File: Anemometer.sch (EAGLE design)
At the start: 1 part, among them IC1 TINY2313-*S*

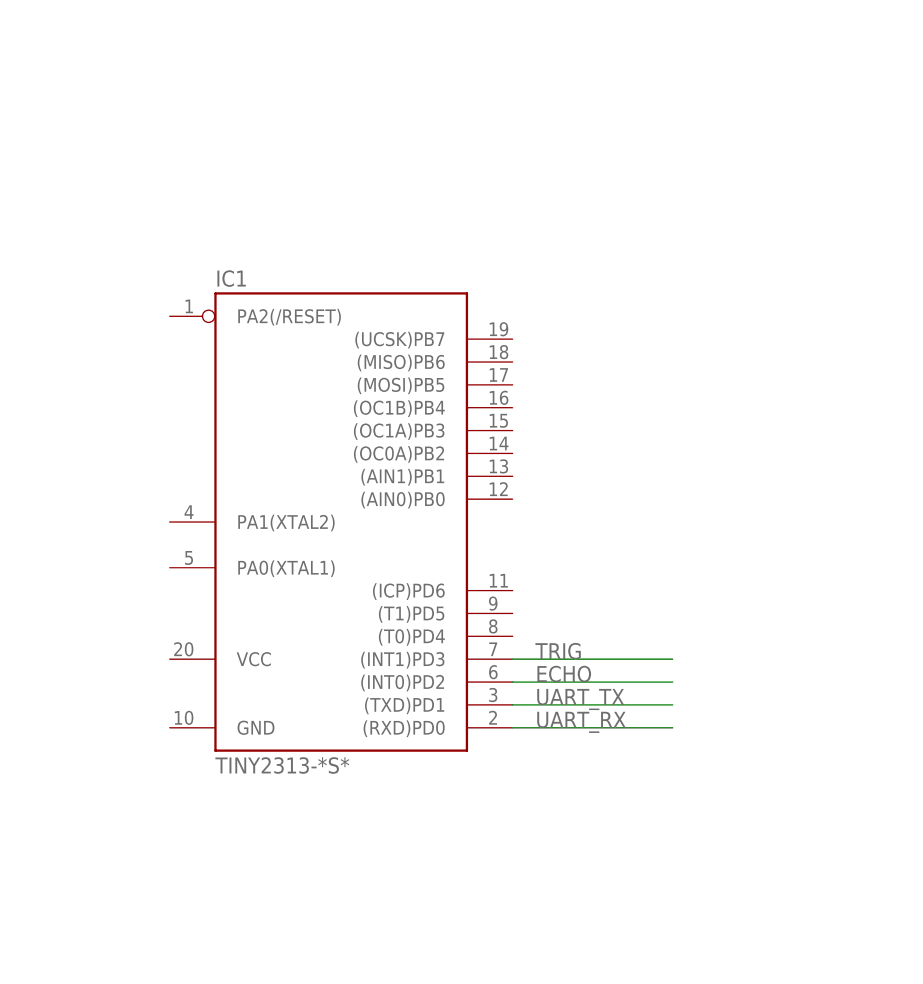
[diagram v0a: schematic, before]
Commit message: added Houskeeping to Schematic
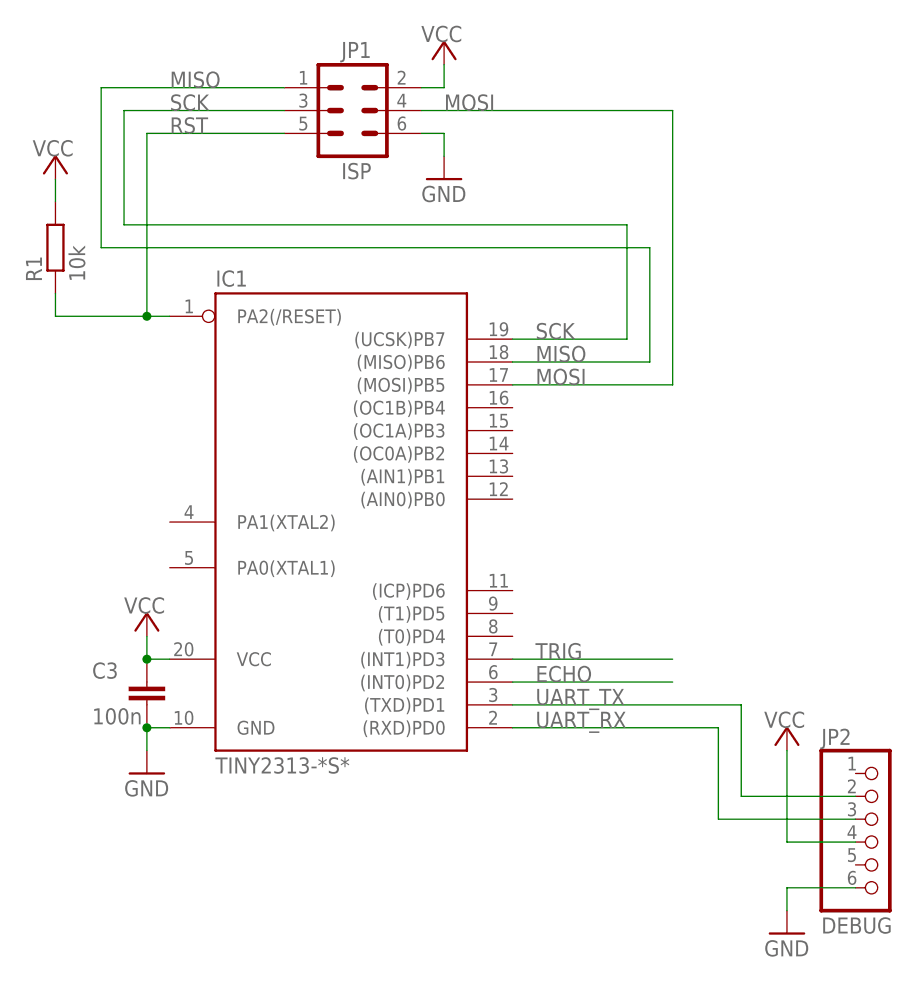
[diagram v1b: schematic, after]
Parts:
- added C3: 100n, rcl:C-EU050-024X044
- added JP1: ISP, con-harting-ml:ML6
- added JP2: DEBUG, pinhead:PINHD-1X6
- added R1: 10k, rcl:R-EU_0207/10
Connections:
- new net GND: C3.2, IC1.GND, JP1.6, JP2.6
- new net MISO: IC1.(MISO)PB6, JP1.1
- new net MOSI: IC1.(MOSI)PB5, JP1.4
- new net RST: IC1.PA2(/RESET), JP1.5, R1.1
- new net SCK: IC1.(UCSK)PB7, JP1.3
- new net VCC: C3.1, IC1.VCC, JP1.2, JP2.4, R1.2
- net UART_RX: now also JP2.3
- net UART_TX: now also JP2.2
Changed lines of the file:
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@@
 <parts>
 <part name="IC1" library="avr-7" deviceset="TINY2313*" device="-*S*"/>
+<part name="JP1" library="con-harting-ml" library_urn="urn:adsk.eagle:library:149" deviceset="ML6" device="" package3d_urn="urn:adsk.eagle:package:6988/1" value="ISP"/>
+<part name="R1" library="rcl" library_urn="urn:adsk.eagle:library:334" deviceset="R-EU_" device="0207/10" package3d_urn="urn:adsk.eagle:package:23491/2" value="10k"/>
+<part name="GND1" library="supply1" library_urn="urn:adsk.eagle:library:371" deviceset="GND" device=""/>
+<part name="GND2" library="supply1" library_urn="urn:adsk.eagle:library:371" deviceset="GND" device=""/>
+<part name="P+1" library="supply1" library_urn="urn:adsk.eagle:library:371" deviceset="VCC" device=""/>
+<part name="P+2" library="supply1" library_urn="urn:adsk.eagle:library:371" deviceset="VCC" device=""/>
+<part name="P+3" library="supply1" library_urn="urn:adsk.eagle:library:371" deviceset="VCC" device=""/>
+<part name="JP2" library="pinhead" library_urn="urn:adsk.eagle:library:325" deviceset="PINHD-1X6" device="" package3d_urn="urn:adsk.eagle:package:22472/2" value="DEBUG"/>
+<part name="GND3" library="supply1" library_urn="urn:adsk.eagle:library:371" deviceset="GND" device=""/>
+<part name="P+4" library="supply1" library_urn="urn:adsk.eagle:library:371" deviceset="VCC" device=""/>
+<part name="C3" library="rcl" library_urn="urn:adsk.eagle:library:334" deviceset="C-EU" device="050-024X044" package3d_urn="urn:adsk.eagle:package:23643/1" value="100n"/>
 </parts>
 <sheets>
@@
 <attribute name="NAME" x="-15.24" y="23.622" size="1.778" layer="95"/>
 </instance>
+<instance part="JP1" gate="1" x="0" y="43.18" smashed="yes" rot="R180">
+<attribute name="VALUE" x="-1.27" y="35.56" size="1.778" layer="96"/>
+<attribute name="NAME" x="-1.27" y="49.022" size="1.778" layer="95"/>
+</instance>
+<instance part="R1" gate="G$1" x="-33.02" y="27.94" smashed="yes" rot="R90">
+<attribute name="NAME" x="-34.5186" y="24.13" size="1.778" layer="95" rot="R90"/>
+<attribute name="VALUE" x="-29.718" y="24.13" size="1.778" layer="96" rot="R90"/>
+</instance>
+<instance part="GND1" gate="1" x="-22.86" y="-30.48" smashed="yes">
+<attribute name="VALUE" x="-25.4" y="-33.02" size="1.778" layer="96"/>
+</instance>
+<instance part="GND2" gate="1" x="10.16" y="35.56" smashed="yes">
+<attribute name="VALUE" x="7.62" y="33.02" size="1.778" layer="96"/>
+</instance>
+<instance part="P+1" gate="VCC" x="-33.02" y="38.1" smashed="yes">
+<attribute name="VALUE" x="-35.56" y="38.1" size="1.778" layer="96"/>
+</instance>
+<instance part="P+2" gate="VCC" x="10.16" y="50.8" smashed="yes">
+<attribute name="VALUE" x="7.62" y="50.8" size="1.778" layer="96"/>
+</instance>
+<instance part="P+3" gate="VCC" x="-22.86" y="-12.7" smashed="yes">
+<attribute name="VALUE" x="-25.4" y="-12.7" size="1.778" layer="96"/>
+</instance>
+<instance part="JP2" gate="A" x="58.42" y="-38.1" smashed="yes">
+<attribute name="NAME" x="52.07" y="-27.305" size="1.778" layer="95"/>
+<attribute name="VALUE" x="52.07" y="-48.26" size="1.778" layer="96"/>
+</instance>
+<instance part="GND3" gate="1" x="48.26" y="-48.26" smashed="yes">
+<attribute name="VALUE" x="45.72" y="-50.8" size="1.778" layer="96"/>
+</instance>
+<instance part="P+4" gate="VCC" x="48.26" y="-25.4" smashed="yes">
+<attribute name="VALUE" x="45.72" y="-25.4" size="1.778" layer="96"/>
+</instance>
+<instance part="C3" gate="G$1" x="-22.86" y="-20.32" smashed="yes">
+<attribute name="NAME" x="-28.956" y="-19.939" size="1.778" layer="95"/>
+<attribute name="VALUE" x="-28.956" y="-25.019" size="1.778" layer="96"/>
+</instance>
 </instances>
 <busses>
@@
 <segment>
 <pinref part="IC1" gate="G$1" pin="(TXD)PD1"/>
-<wire x1="17.78" y1="-22.86" x2="35.56" y2="-22.86" width="0.1524" layer="91"/>
+<wire x1="17.78" y1="-22.86" x2="43.18" y2="-22.86" width="0.1524" layer="91"/>
 <label x="20.32" y="-22.86" size="1.778" layer="95"/>
+<pinref part="JP2" gate="A" pin="2"/>
+<wire x1="55.88" y1="-33.02" x2="43.18" y2="-33.02" width="0.1524" layer="91"/>
+<wire x1="43.18" y1="-33.02" x2="43.18" y2="-22.86" width="0.1524" layer="91"/>
 </segment>
 </net>
@@
 <segment>
 <pinref part="IC1" gate="G$1" pin="(RXD)PD0"/>
-<wire x1="17.78" y1="-25.4" x2="35.56" y2="-25.4" width="0.1524" layer="91"/>
+<wire x1="17.78" y1="-25.4" x2="40.64" y2="-25.4" width="0.1524" layer="91"/>
 <label x="20.32" y="-25.4" size="1.778" layer="95"/>
+<pinref part="JP2" gate="A" pin="3"/>
+<wire x1="55.88" y1="-35.56" x2="40.64" y2="-35.56" width="0.1524" layer="91"/>
+<wire x1="40.64" y1="-35.56" x2="40.64" y2="-25.4" width="0.1524" layer="91"/>
+</segment>
+</net>
+<net name="MISO" class="0">
+<segment>
+<pinref part="JP1" gate="1" pin="1"/>
+<wire x1="-7.62" y1="45.72" x2="-27.94" y2="45.72" width="0.1524" layer="91"/>
+<label x="-20.32" y="45.72" size="1.778" layer="95"/>
+<wire x1="17.78" y1="15.24" x2="33.02" y2="15.24" width="0.1524" layer="91"/>
+<wire x1="33.02" y1="15.24" x2="33.02" y2="27.94" width="0.1524" layer="91"/>
+<wire x1="33.02" y1="27.94" x2="-27.94" y2="27.94" width="0.1524" layer="91"/>
+<wire x1="-27.94" y1="27.94" x2="-27.94" y2="45.72" width="0.1524" layer="91"/>
+<label x="20.32" y="15.24" size="1.778" layer="95"/>
+<pinref part="IC1" gate="G$1" pin="(MISO)PB6"/>
+</segment>
+</net>
+<net name="SCK" class="0">
+<segment>
+<pinref part="JP1" gate="1" pin="3"/>
+<wire x1="-7.62" y1="43.18" x2="-25.4" y2="43.18" width="0.1524" layer="91"/>
+<label x="-20.32" y="43.18" size="1.778" layer="95"/>
+<wire x1="17.78" y1="17.78" x2="30.48" y2="17.78" width="0.1524" layer="91"/>
+<wire x1="30.48" y1="17.78" x2="30.48" y2="30.48" width="0.1524" layer="91"/>
+<wire x1="30.48" y1="30.48" x2="-25.4" y2="30.48" width="0.1524" layer="91"/>
+<wire x1="-25.4" y1="30.48" x2="-25.4" y2="43.18" width="0.1524" layer="91"/>
+<label x="20.32" y="17.78" size="1.778" layer="95"/>
+<pinref part="IC1" gate="G$1" pin="(UCSK)PB7"/>
+</segment>
+</net>
+<net name="RST" class="0">
+<segment>
+<pinref part="JP1" gate="1" pin="5"/>
+<wire x1="-7.62" y1="40.64" x2="-22.86" y2="40.64" width="0.1524" layer="91"/>
+<label x="-20.32" y="40.64" size="1.778" layer="95"/>
+<wire x1="-20.32" y1="20.32" x2="-22.86" y2="20.32" width="0.1524" layer="91"/>
+<wire x1="-22.86" y1="20.32" x2="-22.86" y2="40.64" width="0.1524" layer="91"/>
+<pinref part="R1" gate="G$1" pin="1"/>
+<wire x1="-33.02" y1="22.86" x2="-33.02" y2="20.32" width="0.1524" layer="91"/>
+<wire x1="-33.02" y1="20.32" x2="-22.86" y2="20.32" width="0.1524" layer="91"/>
+<junction x="-22.86" y="20.32"/>
+<pinref part="IC1" gate="G$1" pin="PA2(/RESET)"/>
+</segment>
+</net>
+<net name="MOSI" class="0">
+<segment>
+<pinref part="JP1" gate="1" pin="4"/>
+<wire x1="7.62" y1="43.18" x2="35.56" y2="43.18" width="0.1524" layer="91"/>
+<label x="10.16" y="43.18" size="1.778" layer="95"/>
+<wire x1="17.78" y1="12.7" x2="35.56" y2="12.7" width="0.1524" layer="91"/>
+<wire x1="35.56" y1="12.7" x2="35.56" y2="43.18" width="0.1524" layer="91"/>
+<label x="20.32" y="12.7" size="1.778" layer="95"/>
+<pinref part="IC1" gate="G$1" pin="(MOSI)PB5"/>
+</segment>
+</net>
+<net name="GND" class="0">
+<segment>
+<pinref part="GND1" gate="1" pin="GND"/>
+<wire x1="-22.86" y1="-27.94" x2="-22.86" y2="-25.4" width="0.1524" layer="91"/>
+<wire x1="-22.86" y1="-25.4" x2="-20.32" y2="-25.4" width="0.1524" layer="91"/>
+<pinref part="C3" gate="G$1" pin="2"/>
+<junction x="-22.86" y="-25.4"/>
+<pinref part="IC1" gate="G$1" pin="GND"/>
+</segment>
+<segment>
+<pinref part="JP1" gate="1" pin="6"/>
+<pinref part="GND2" gate="1" pin="GND"/>
+<wire x1="7.62" y1="40.64" x2="10.16" y2="40.64" width="0.1524" layer="91"/>
+<wire x1="10.16" y1="40.64" x2="10.16" y2="38.1" width="0.1524" layer="91"/>
+</segment>
+<segment>
+<pinref part="JP2" gate="A" pin="6"/>
+<pinref part="GND3" gate="1" pin="GND"/>
+<wire x1="55.88" y1="-43.18" x2="48.26" y2="-43.18" width="0.1524" layer="91"/>
+<wire x1="48.26" y1="-43.18" x2="48.26" y2="-45.72" width="0.1524" layer="91"/>
+</segment>
+</net>
+<net name="VCC" class="0">
+<segment>
+<pinref part="P+3" gate="VCC" pin="VCC"/>
+<wire x1="-20.32" y1="-17.78" x2="-22.86" y2="-17.78" width="0.1524" layer="91"/>
+<wire x1="-22.86" y1="-17.78" x2="-22.86" y2="-15.24" width="0.1524" layer="91"/>
+<pinref part="C3" gate="G$1" pin="1"/>
+<junction x="-22.86" y="-17.78"/>
+<pinref part="IC1" gate="G$1" pin="VCC"/>
+</segment>
+<segment>
+<pinref part="R1" gate="G$1" pin="2"/>
+<pinref part="P+1" gate="VCC" pin="VCC"/>
+<wire x1="-33.02" y1="33.02" x2="-33.02" y2="35.56" width="0.1524" layer="91"/>
+</segment>
+<segment>
+<pinref part="JP1" gate="1" pin="2"/>
+<pinref part="P+2" gate="VCC" pin="VCC"/>
+<wire x1="7.62" y1="45.72" x2="10.16" y2="45.72" width="0.1524" layer="91"/>
+<wire x1="10.16" y1="45.72" x2="10.16" y2="48.26" width="0.1524" layer="91"/>
+</segment>
+<segment>
+<pinref part="JP2" gate="A" pin="4"/>
+<pinref part="P+4" gate="VCC" pin="VCC"/>
+<wire x1="55.88" y1="-38.1" x2="48.26" y2="-38.1" width="0.1524" layer="91"/>
+<wire x1="48.26" y1="-38.1" x2="48.26" y2="-27.94" width="0.1524" layer="91"/>
 </segment>
 </net>
@@
 </schematic>
 </drawing>
+<compatibility>
+<note version="8.2" severity="warning">
+Since Version 8.2, EAGLE supports online libraries. The ids
+of those online libraries will not be understood (or retained)
+with this version.
+</note>
+<note version="8.3" severity="warning">
+Since Version 8.3, EAGLE supports URNs for individual library
+assets (packages, symbols, and devices). The URNs of those assets
+will not be understood (or retained) with this version.
+</note>
+<note version="8.3" severity="warning">
+Since Version 8.3, EAGLE supports the association of 3D packages
+with devices in libraries, schematics, and board files. Those 3D
+packages will not be understood (or retained) with this version.
+</note>
+</compatibility>
 </eagle>

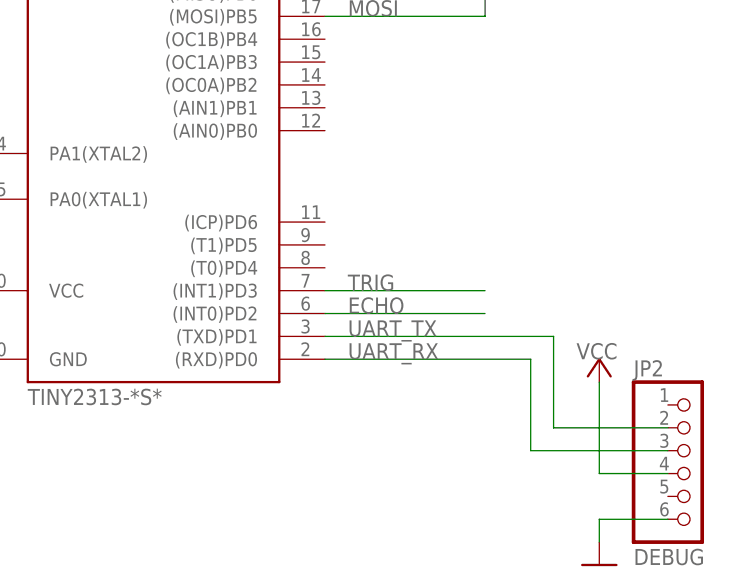
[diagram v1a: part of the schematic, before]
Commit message: changed timekeeping to hardware timer
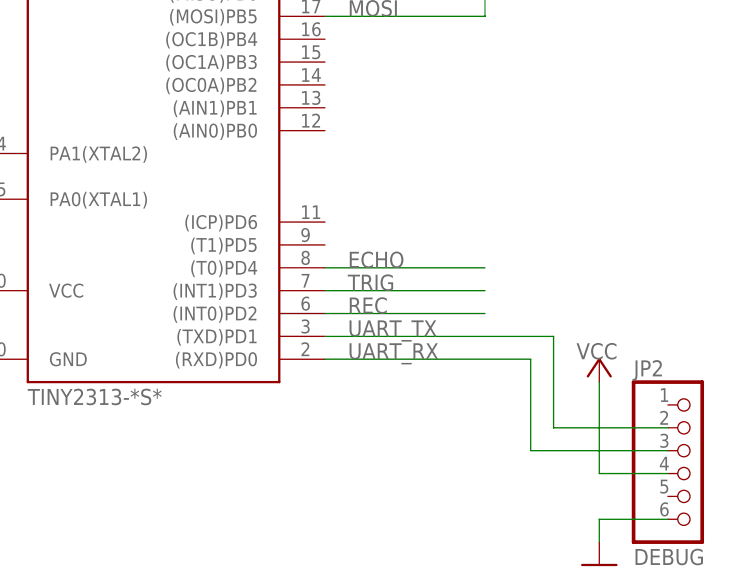
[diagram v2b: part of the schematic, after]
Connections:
- new net REC: IC1.(INT0)PD2
- net ECHO: now also IC1.(T0)PD4; no longer IC1.(INT0)PD2
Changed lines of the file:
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@@
 </busses>
 <nets>
-<net name="ECHO" class="0">
+<net name="REC" class="0">
 <segment>
 <pinref part="IC1" gate="G$1" pin="(INT0)PD2"/>
@@
 </segment>
 </net>
+<net name="ECHO" class="0">
+<segment>
+<pinref part="IC1" gate="G$1" pin="(T0)PD4"/>
+<wire x1="17.78" y1="-15.24" x2="35.56" y2="-15.24" width="0.1524" layer="91"/>
+<label x="20.32" y="-15.24" size="1.778" layer="95"/>
+</segment>
+</net>

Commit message: added input Logic to Schematic
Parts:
- added C1, C2: 100n, rcl:C-EUC0805
- added IC2, IC3: 74HC151D, 74xx-us:74LS151D
- added IC4: 74HC08D, 74xx-us:74ALS08D
- added IC5: LM555D, linear:LM555D
- added IC6: 74LS138D, 74xx-us:74LS138D
- added IC7: 74HC04D, 74xx-eu:74HC04D
- added JP3: X+, pinhead:PINHD-1X5
- added JP4: X-, pinhead:PINHD-1X5
- added JP5: Y+, pinhead:PINHD-1X5
- added JP6: Y-, pinhead:PINHD-1X5
- added JP7: Z+, pinhead:PINHD-1X5
- added JP8: Z-, pinhead:PINHD-1X5
- added R2: 22k, rcl:R-EU_R0805
- added R3, R4, R5, R6, R7, R8, R9: 10k, rcl:R-EU_R0805
- JP2: value DEBUG -> UART
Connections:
- new net A: IC2A.A, IC3A.A, IC6A.A
- new net B: IC2A.B, IC3A.B, IC6A.B
- new net C: IC2A.C, IC3A.C, IC6A.C
- new net ECHO_1: IC3A.D0, JP3.3
- new net ECHO_2: IC3A.D1, JP4.3
- new net ECHO_3: IC3A.D2, JP5.3
- new net ECHO_4: IC3A.D3, JP6.3
- new net ECHO_5: IC3A.D4, JP7.3
- new net ECHO_6: IC3A.D5, JP8.3
- new net N$1: IC5.Q, IC7A.I, R9.1
- new net N$2: C1.1, IC5.CV
- new net N$4: C2.1, IC5.DIS, IC5.THR, R2.1
- new net N$5: IC4A.I0, IC7A.O
- new net N$7: IC4A.O, IC4B.I0
- new net PULS: IC1.(ICP)PD6, IC4B.O
- new net REC_1: IC2A.D1, JP3.5, R4.2
- new net REC_2: IC2A.D0, JP4.5, R3.2
- new net REC_3: IC2A.D3, JP5.5, R6.2
- new net REC_4: IC2A.D2, JP6.5, R5.2
- new net REC_5: IC2A.D5, JP7.5, R8.2
- new net REC_6: IC2A.D4, JP8.5, R7.2
- new net TRIG_1: IC6A.Y0, JP3.2
- new net TRIG_2: IC6A.Y1, JP4.2
- new net TRIG_3: IC6A.Y2, JP5.2
- new net TRIG_4: IC6A.Y3, JP6.2
- new net TRIG_5: IC6A.Y4, JP7.2
- new net TRIG_6: IC6A.Y5, JP8.2
- net ECHO: now also IC3A.Y, IC4A.I1; no longer IC1.(T0)PD4
- net GND: now also C1.2, C2.2, IC2A.D6, IC2A.D7, IC2A.G, IC3A.D6, IC3A.D7, IC3A.G, IC5.GND, IC6A.G2A, IC6A.G2B, JP3.4, JP4.4, JP5.4, JP6.4, JP7.4, JP8.4, R3.1, R4.1, R5.1, R6.1, R7.1, R8.1
- net REC: now also IC2A.Y, IC5.TR; no longer IC1.(INT0)PD2
- net TRIG: now also IC6A.G1
- net VCC: now also IC4B.I1, IC5.R, IC5.V+, JP3.1, JP4.1, JP5.1, JP6.1, JP7.1, JP8.1, R2.2, R9.2
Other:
- note added: "X"
- note added: "Y"
- note added: "Z"

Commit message: changed messurment methode to half external counter
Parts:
- removed R9: 10k, rcl:R-EU_R0805
- added C4, C5: 20p, rcl:C-EUC0805
- added IC8: 74HC393D, 74xx-us:74LS393D
- added Q1: 16MHz, crystal:CRYSTALHC49UP
- IC6: value 74LS138D -> 74HC138D
- IC7: value 74HC04D -> 74ALS04D; device 74xx-eu:74HC04D -> 74xx-us:74ALS04D
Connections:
- new net 16MHZ: IC4B.I0, IC7B.O
- new net N$3: IC4B.O, IC8A.A
- new net N$6: C4.1, IC7A.I, Q1.1
- new net PULS*2: IC1.(T0)PD4, IC8A.QA
- new net TIME: IC1.(ICP)PD6, IC4A.O, IC4B.I1
- net A: now also IC1.(AIN0)PB0
- net B: now also IC1.(AIN1)PB1
- net C: now also IC1.(OC0A)PB2
- net ECHO: now also IC4A.I0; no longer IC4A.I1
- net GND: now also C4.2, C5.2, IC2P.GND, IC3P.GND, IC4C.I0, IC4C.I1, IC4D.I0, IC4D.I1, IC4P.GND, IC6P.GND, IC7D.I, IC7E.I, IC7F.I, IC7P.GND, IC8B.A, IC8B.CLR, IC8P.GND
- net N$1: now also IC7C.I; no longer IC7A.I, R9.1
- net N$5: now also IC4A.I1, IC7C.O; no longer IC4A.I0, IC7A.O
- net N$7: now also C5.1, IC7A.O, IC7B.I, Q1.2; no longer IC4A.O, IC4B.I0
- net PULS: now also IC1.(T1)PD5, IC8A.QB; no longer IC1.(ICP)PD6, IC4B.O
- net TRIG: now also IC8A.CLR
- net VCC: now also IC2P.VCC, IC3P.VCC, IC4P.VCC, IC6P.VCC, IC7P.VCC, IC8P.VCC; no longer IC4B.I1, R9.2
